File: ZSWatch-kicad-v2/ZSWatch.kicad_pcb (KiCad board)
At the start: 4 copper layers, 41 x 38 mm, 76 parts, among them IC1 ESDALC6V1W5, IC2 XC9265C181MR-G, IC3 TPS61023DRLT, IC4 MAX30101EFD+T, IC5 FAN5622SX, IC6 BMI270, IC7 LIS2MDLTR, J2 Charger and programming heade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, M1 Vibrator DC Motor, U1 MAX1811ESA+, U10 0_NORA-B106, U11 TXB0104QRUTRQ1, U12 GC9A01, U13 GC9A01A_CST816S, U2 DMC2400UV-7, U3 NCV300LSN36T1G, U4 BMP581, U5 BME688, U6 DRV2603RUNT, U7 XC9265A331MR-G

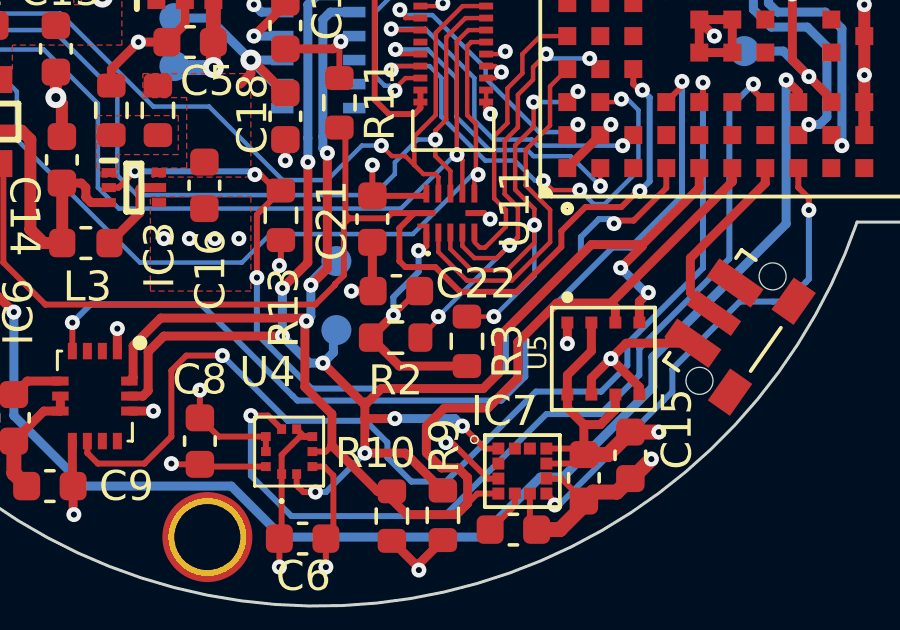
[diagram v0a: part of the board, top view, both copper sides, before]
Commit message: Replace touch chip logic shifter with one that works with I2C.
Replace TXB0104 with pin compatible NTS0104GU12. It includes internal
pullups hence the touch I2C pin pullups are removed.

For ZSWatch without touch screen then we may still mount TXB0104 as I can see
there may be some current leakage when running SPI and using NTS0104 due to it's
internal pullups. Will test this later.
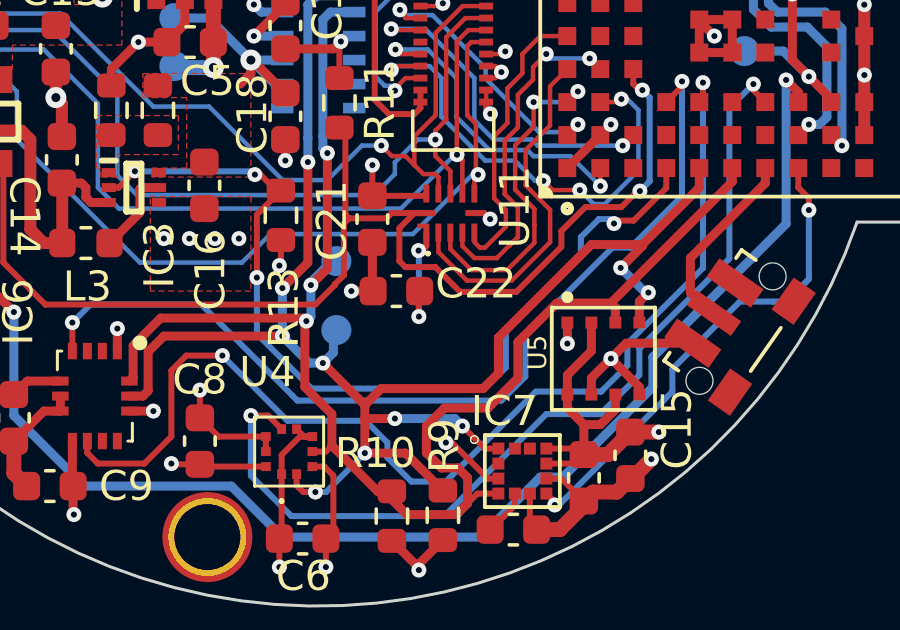
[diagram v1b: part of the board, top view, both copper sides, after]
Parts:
- removed R2, R3: 4.7k, Resistor_SMD:R_0603_1608Metric
- U11: value TXB0104QRUTRQ1 -> TXB0104QRUTRQ1/NTS0104GU12
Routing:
- net +1V8: track 64.0 -> 58.7 mm
- net TOUCH_SCL: track 15.9 -> 11.3 mm, vias 4 -> 2
- net TOUCH_SDA: track 15.9 -> 11.6 mm, vias 4 -> 2

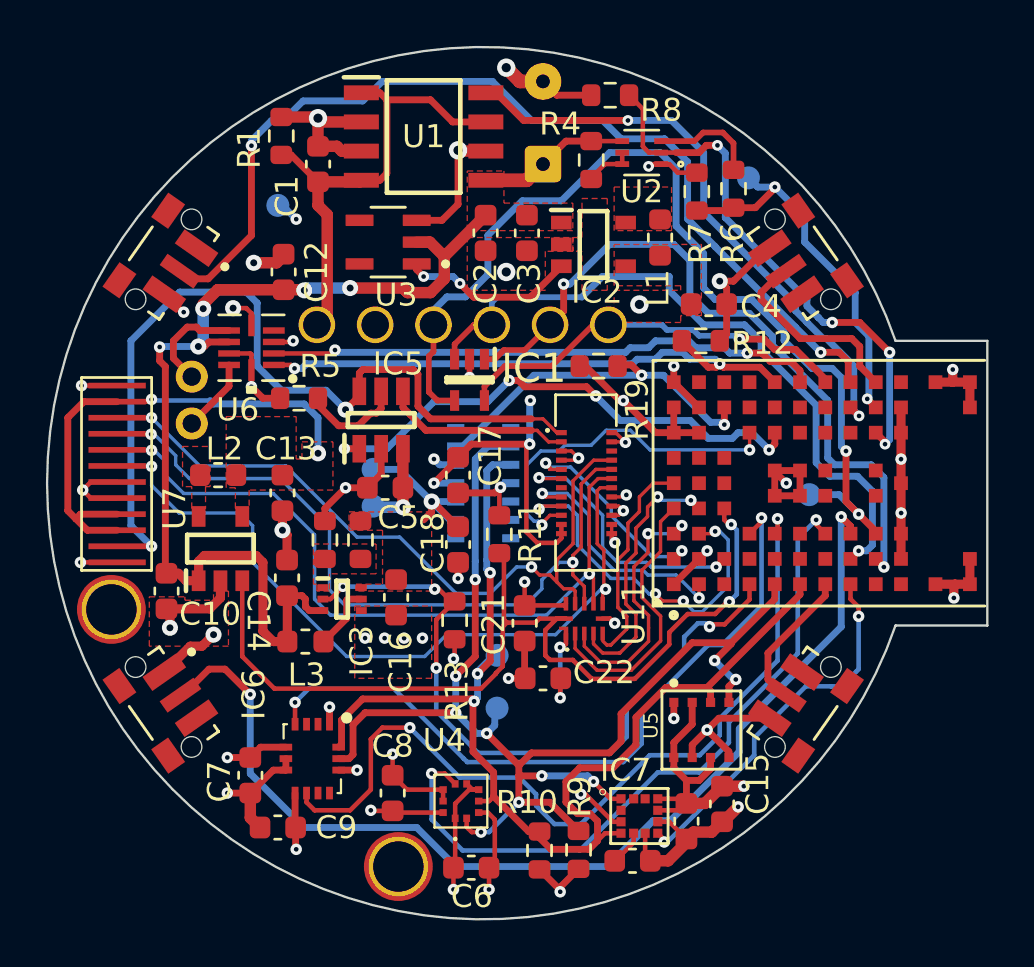
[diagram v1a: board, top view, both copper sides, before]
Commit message: Move display connector so there is no strain on the cable. From now on only touch screen is supported. Remove none touch screen connector as it does not fit anymore.
The moving of touch display connector caused a bit of re-routing. Without redoing alot of the routing
we need the space used by the connector to the none touch screen. From now on only touch screen is supported.
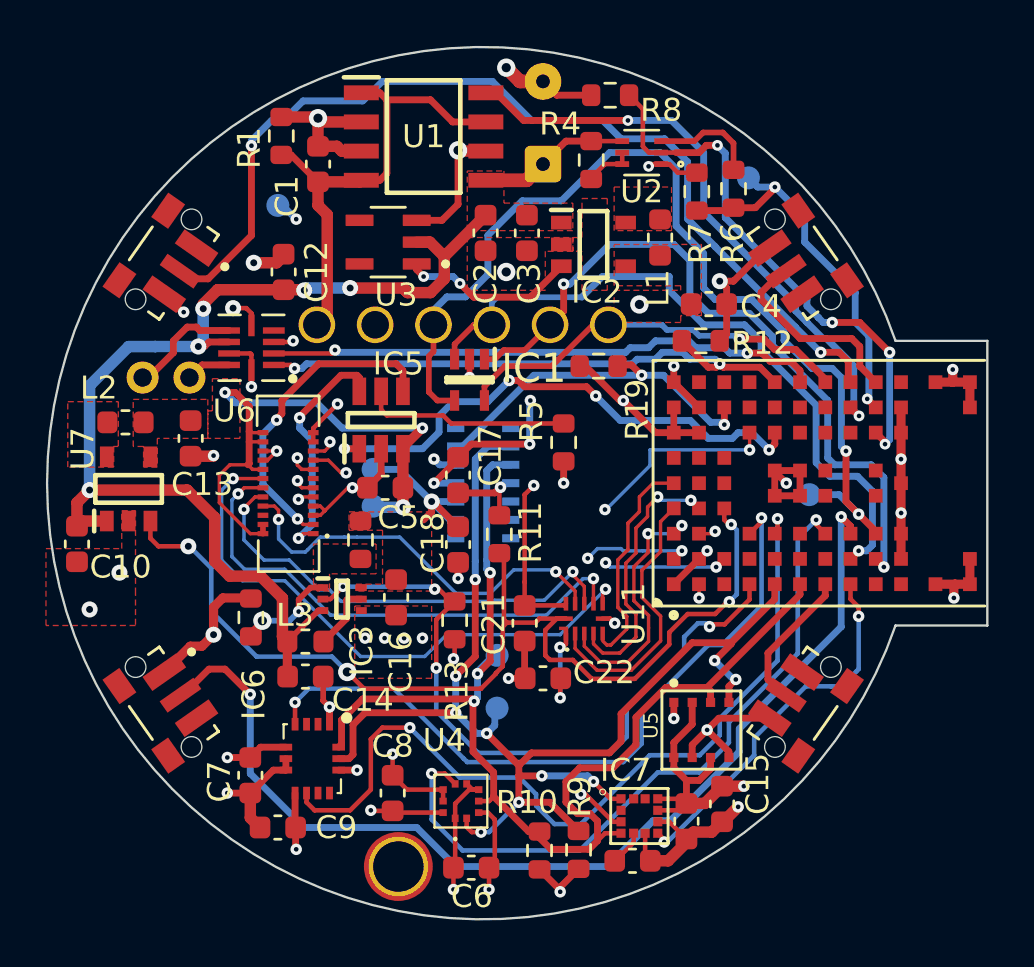
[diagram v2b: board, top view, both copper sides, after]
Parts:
- removed H2: MountingHole, MountingHole:MountingHole_2.2mm_M2_DIN965_Pad_TopOnly
- removed U12: GC9A01, user_library:GC9A01_disp_smaller
- moved U13 13.0 mm to (89.4, 100.4), turned to 90 degrees
- moved R5 11.7 mm to (101.4, 98.6), turned to 90 degrees
- moved U7 4.77 mm to (82.5, 100.7)
- moved R18 4.67 mm to (87.8, 106.2)
- moved C13 4.65 mm to (85.2, 98.5)
- moved L2 4.65 mm to (82.3, 97.8)
- moved C10 4.41 mm to (80.2, 103.0)
- moved C14 4.37 mm to (90.2, 108.8), turned to 0 degrees
- moved M1 2.00 mm to (85.1, 95.8), turned to 180 degrees
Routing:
- net LEDK1: track 37.5 -> 10.5 mm
- net /TOUCH_HIGH_INT-DC: track 31.4 -> 17.8 mm
- net /TOUCH_HIGH_SCL-CS: track 32.9 -> 20.0 mm
- net DISPLAY_CLK: track 11.0 -> 21.8 mm
- net /TOUCH_HIGH_SDA-SCL: track 32.6 -> 22.6 mm
- net DISPLAY_DC: track 9.31 -> 19.2 mm, vias 2 -> 3
- net DISPLAY_DATA: track 11.6 -> 21.2 mm, vias 2 -> 3
- net GND: track 117.1 -> 108.6 mm, vias 45 -> 43
- net DISPLAY_RST: track 15.5 -> 23.9 mm, vias 2 -> 3
- net /TOUCH_HIGH_RST-SDA: track 33.0 -> 25.4 mm
- net DISPLAY_3V3: track 31.2 -> 38.8 mm, vias 7 -> 4
- net LEDK2: track 8.22 -> 13.9 mm, vias 0 -> 2
- net V_BAT: track 51.5 -> 56.8 mm
- net DISPLAY_CS: track 15.9 -> 20.9 mm, vias 4 -> 2
- net DISPLAY_EN: track 40.3 -> 44.9 mm, vias 2 -> 4
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- removed copper zone on In2.Cu, net DISPLAY_3V3

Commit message: Minor tidy up of v2 PCB and improved silkscreen.
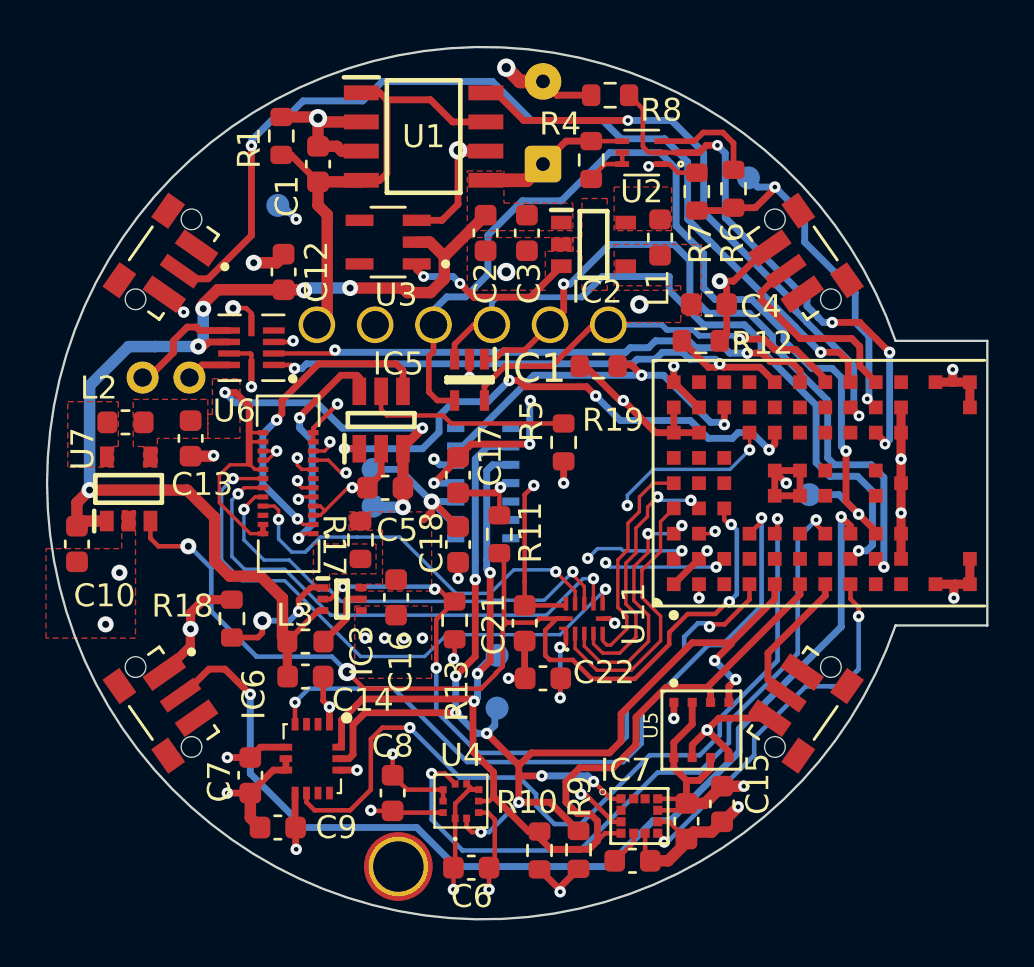
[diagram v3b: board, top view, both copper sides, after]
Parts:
- added G***: LOGO, LOGO, B.Cu at (83.5, 99.8)
- moved R18 0.83 mm to (87.0, 106.3)
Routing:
- net /TPS_FB: track 4.43 -> 5.48 mm
- net GND: track 108.6 -> 107.9 mm
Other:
- board text added: "GPIO"
- board text added: "RST"
- board text added: "SWDCLK"
- board text added: "SWDIO"
- board text added: "VBUS"
- board text added: "v2 Rev 2"
- board text removed: "v2 Rev 1"

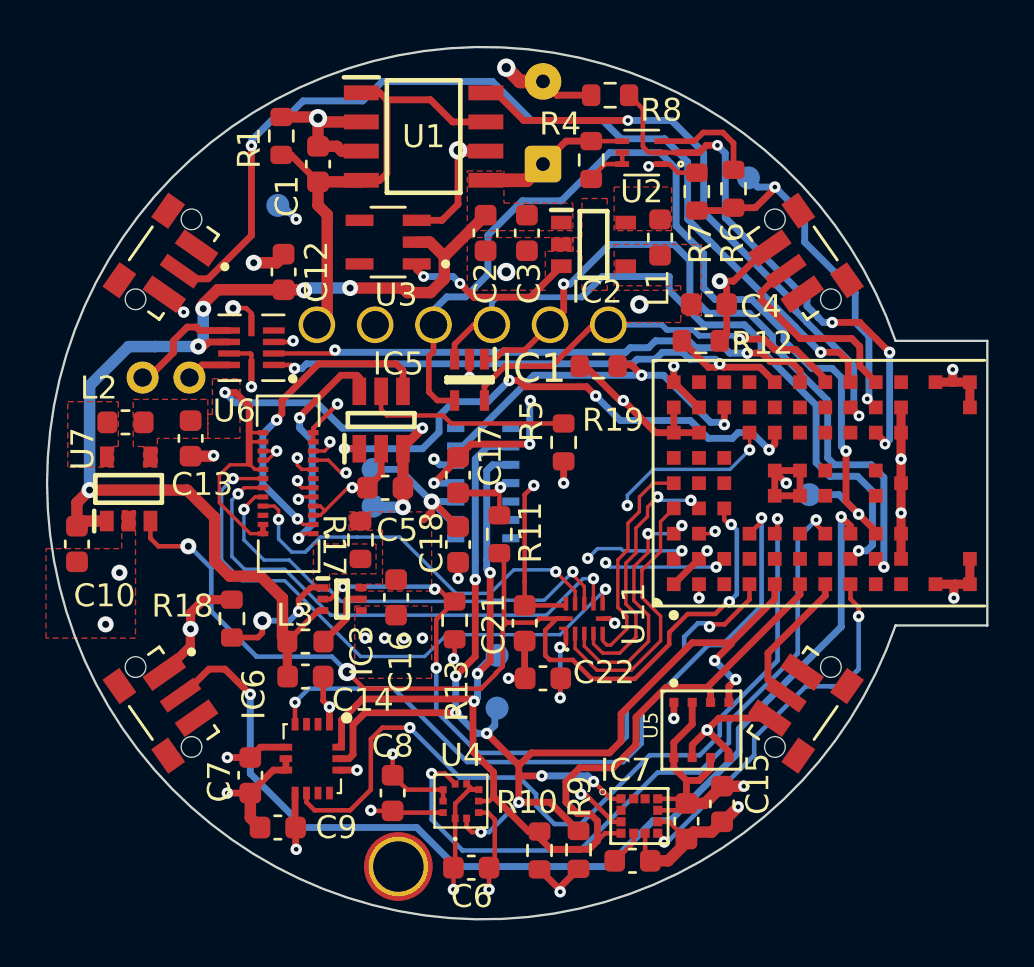
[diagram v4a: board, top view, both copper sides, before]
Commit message: Initial hardware changes to add an external flash (AT25SL128A) to ZSwatch.
Signed-off-by: Victor Chavez <vchavezb@protonmail.com>
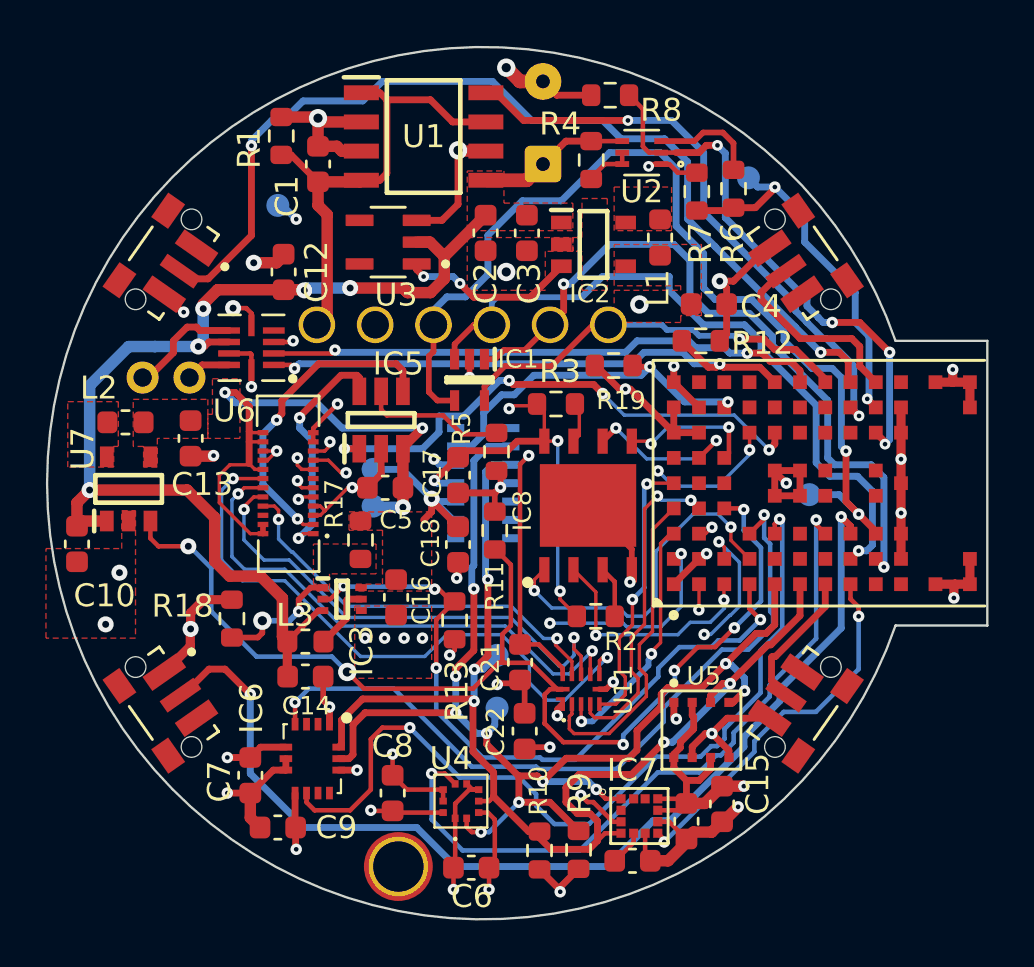
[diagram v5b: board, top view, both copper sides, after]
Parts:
- added IC8: AT25SF128A-MHB-T, flash:SON127P600X500X60-9N-D, F.Cu at (102.5, 101.4)
- added R2: 10k, Resistor_SMD:R_0603_1608Metric, F.Cu at (102.8, 106.2)
- added R3: 10k, Resistor_SMD:R_0603_1608Metric, F.Cu at (101.1, 97.0)
- U11: value TXB0104QRUTRQ1/NTS0104GU12 -> NTS0104GU12
- moved U11 3.08 mm to (102.2, 109.4)
- moved R5 2.95 mm to (98.5, 99.0)
- moved C22 2.44 mm to (99.7, 111.2), turned to -90 degrees
- moved C21 1.71 mm to (99.5, 108.2)
- moved R19 0.66 mm to (103.6, 95.3)
- moved R11 0.26 mm to (98.4, 102.5)
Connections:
- U10 pad B6: unconnected-(U10-PadB6) -> FLASH_CLK
- U10 pad C1: unconnected-(U10-PadC1) -> FLASH_SO
- U10 pad C6: unconnected-(U10-PadC6) -> FLASH_SI
- U10 pad D2: unconnected-(U10-PadD2) -> FLASH_CS
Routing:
- net FLASH_CS: track 0.00 -> 15.3 mm, vias 0 -> 2
- net FLASH_SO: track 0.00 -> 10.4 mm, vias 0 -> 2
- net DISPLAY_3V3: track 38.7 -> 48.0 mm
- net +1V8: track 54.5 -> 61.8 mm, vias 17 -> 18
- net FLASH_CLK: track 0.00 -> 7.15 mm, vias 0 -> 2
- net DISPLAY_DATA: track 21.2 -> 27.7 mm
- net FLASH_SI: track 0.00 -> 6.00 mm, vias 0 -> 2
- net DISPLAY_EN: track 44.9 -> 49.2 mm, vias 4 -> 6
- net GND: track 107.9 -> 111.9 mm
- net DISPLAY_DC: track 19.2 -> 22.7 mm
- net /ISET: track 9.00 -> 6.04 mm
- net TOUCH_RST: track 9.46 -> 12.2 mm, vias 0 -> 2
- net TOUCH_SDA: track 11.6 -> 14.2 mm
- net Net-(IC8-~{WP(I}/O2)): track 0.00 -> 2.41 mm
- net TOUCH_INT: track 12.0 -> 14.2 mm
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
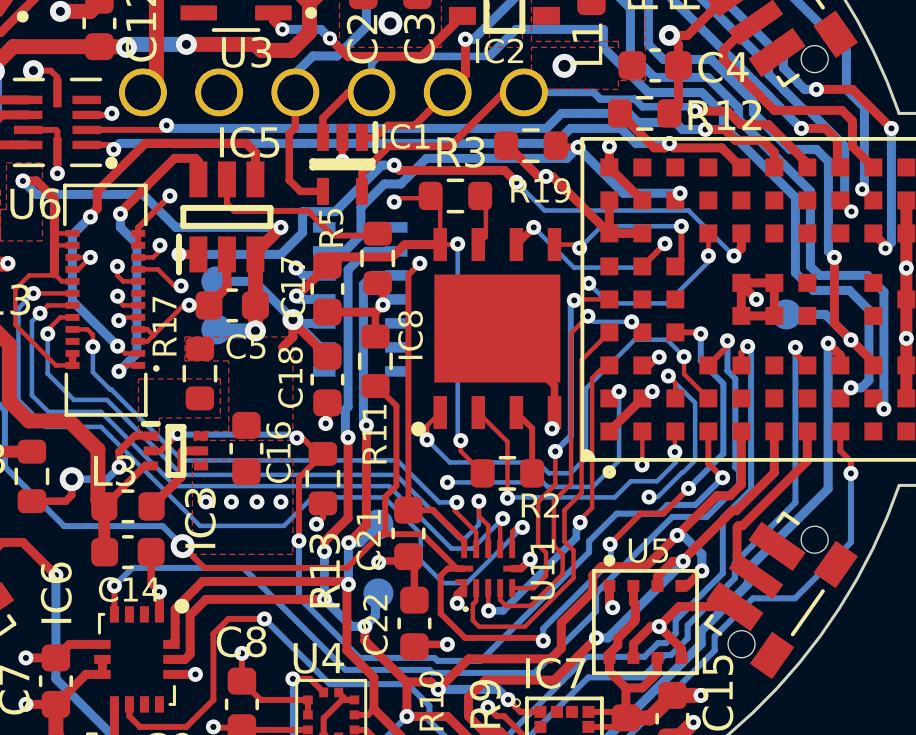
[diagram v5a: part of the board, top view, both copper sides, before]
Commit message: Updated flash pcb design, with DRC rule fixes.
- Lowered down silkscreen of ZWatch to add test points to SPI for testing.
- Ground pad of flash is connected but is not necessary and can be removed
to simplify connections.
- Due to size constraints added 0402 resistors for pull up resistors on the left side
of the flash.
- Pending, change name of FLASH in Kicad to AT25SL128A.
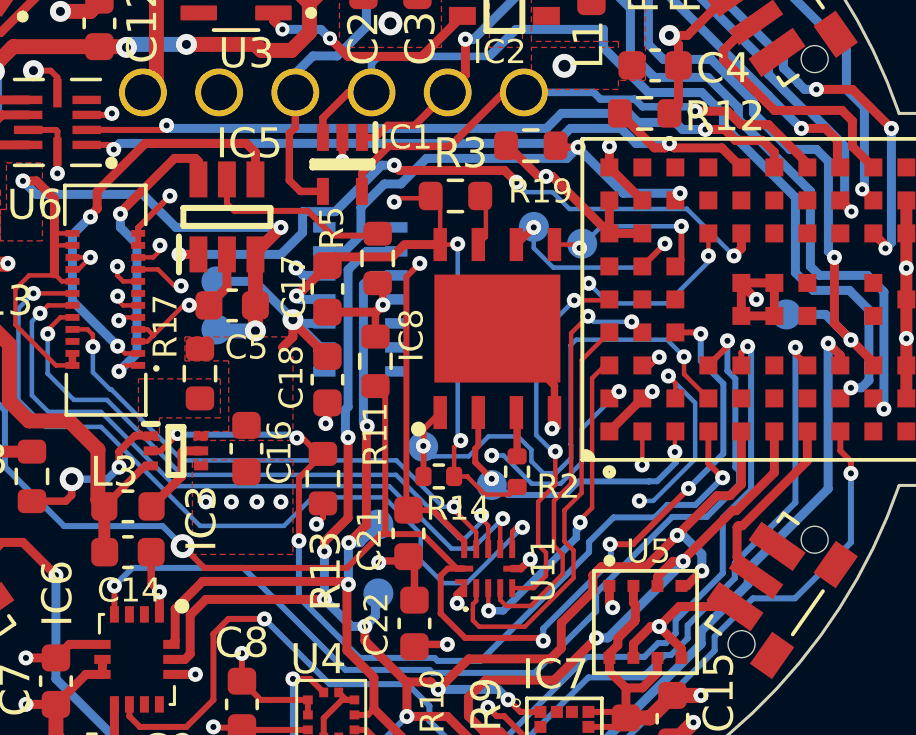
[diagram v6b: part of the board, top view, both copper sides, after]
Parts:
- added CLK: MR, TestPoint:TestPoint_Pad_D1.0mm, B.Cu at (103.7, 98.0)
- added CS: MR, TestPoint:TestPoint_Pad_D1.0mm, B.Cu at (100.0, 105.3)
- added R14: 10k, Resistor_SMD:R_0402_1005Metric, F.Cu at (100.5, 106.3)
- added SI: MR, TestPoint:TestPoint_Pad_D1.0mm, B.Cu at (105.3, 98.5)
- added SO: MR, TestPoint:TestPoint_Pad_D1.0mm, B.Cu at (102.3, 106.6)
- R2: footprint Resistor_SMD:R_0603_1608Metric -> Resistor_SMD:R_0402_1005Metric
- moved G*** 7.49 mm to (97.3, 112.8)
- moved R2 0.33 mm to (103.1, 106.1), turned to -90 degrees
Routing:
- net DISPLAY_3V3: track 48.0 -> 42.6 mm
- net FLASH_CS: track 15.3 -> 18.2 mm
- net +1V8: track 61.8 -> 64.3 mm
- net /TOUCH_HIGH_SCL-CS: track 21.8 -> 20.9 mm
- net Net-(IC8-~{WP(I}/O2)): track 2.41 -> 1.47 mm
- net TOUCH_RST: track 12.2 -> 12.8 mm
- net DISPLAY_DATA: track 27.7 -> 28.2 mm
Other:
- board text added: "v2 Rev 2a"
- board text removed: "v2 Rev 2"
